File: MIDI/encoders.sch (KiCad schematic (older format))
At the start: 47 parts, among them U3 40106, U4 ENCODER_w_SWITCH, U5 ENCODER_w_SWITCH, U6 ENCODER_w_SWITCH

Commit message: Se continuan las correciones correspondientes a la 1ra revisión
> Se realizan los cambios necesarios para la utilización de la biblioteca de huellas autocontenidas.
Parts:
- C10, C11, C12, C13, C14, C15, C16, C4, C5, C6, C7, C8, C9: footprint Capacitors_SMD:C_0603_HandSoldering -> MIDI:C_0805_HandSoldering
- R10, R11, R12, R13, R14, R15, R16, R17, R18, R19, R20, R21, R22, R23, R24, R25, R26, R27, R28, R29, R30, R31, R32, R33, R34, R35, R36, R37, R8, R9: footprint Resistors_SMD:R_0603_HandSoldering -> MIDI:R_0805_HandSoldering
- U3: footprint Housings_DIP:DIP-14_W7.62mm_LongPads -> MIDI:DIP-14_W7.62mm_LongPads

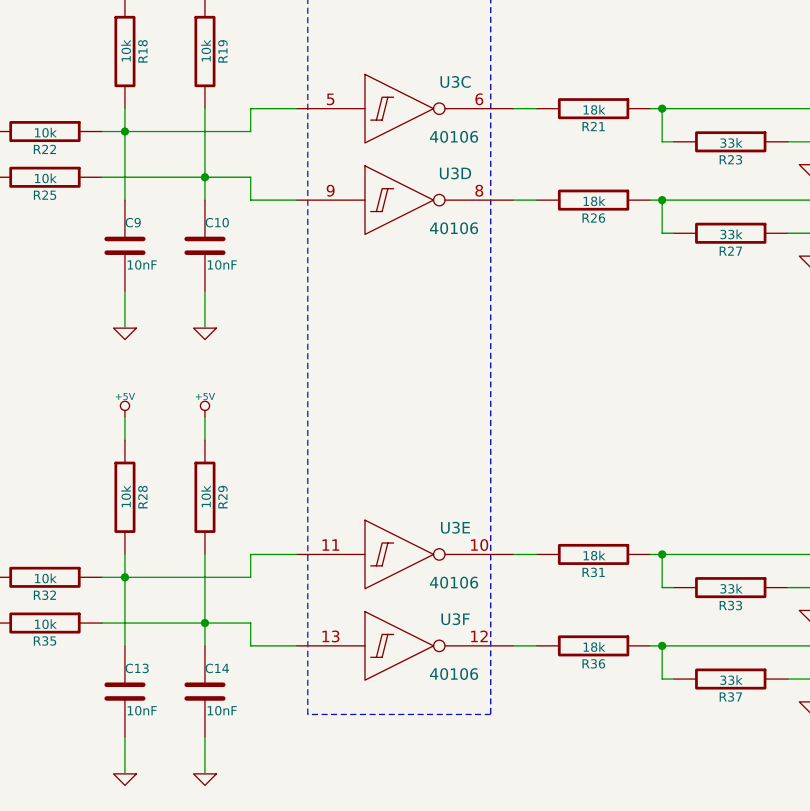
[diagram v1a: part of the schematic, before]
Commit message: Se avanza con primera iteración de ruteo
> Se terminan de rutear conexiones para estudiar factibilidad de placement.
> Para facilitar el ruteo se realizan los siguientes cambios:
  > Se desconecta pin redundante de tact-switch's para permitir la conexión entre planos de masa.
  > Se desconectan pines del conector derecho de forma que no requieran ser ruteados a los homologos del conector izquierdo.
  > Se intercambian unidades F y D del componente 40106.
  > Se agrupan señales de los interruptores de los encoders en vez de intercalarlos con las señales de encoder, propiamente dicho, de cada uno. Se rutean a pines superiores en el conector izquierdo, mientras se desplazan las restantes señales hacia abajo.

> Se aguarda comentarios de los revisores para emprolijar, embellecer y mejorar el ruteo.
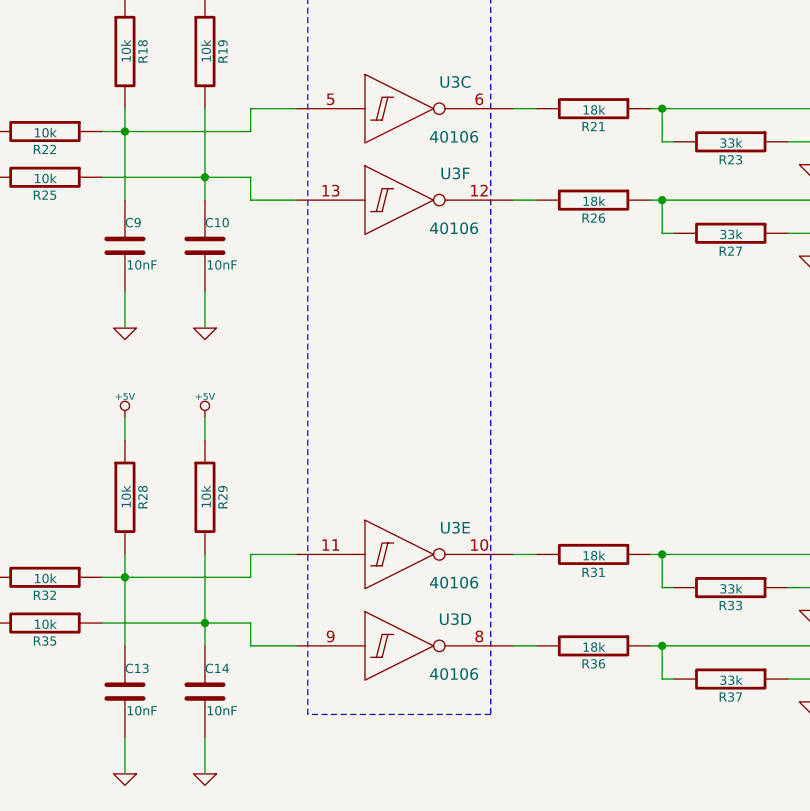
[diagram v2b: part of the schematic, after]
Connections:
- net at U3.8: now also R36.2; no longer R26.2
- net at C10.1, R19.2, R25.1: now also U3.13; no longer U3.9
- net at U3.12: now also R26.2; no longer R36.2
- net at C14.1, R29.2, R35.1: now also U3.9; no longer U3.13
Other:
- moved on the sheet: U3D, U3F

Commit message: Se modifican campos de componentes
> Se realizan los cambios en los campos de kiCost para reflejar los cambios de footprints (de 0603 a 0805).
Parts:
- C10, C13, C14, C5, C6, C9: Desc CAP CER 10000PF 50V X7R 0603 -> CAP CER 10000PF 50V X7R 0805; Digikey# 490-1512-1-ND -> 311-1136-1-ND; Manf Murata Electronics North America -> Yageo; Manf# GRM188R71H103KA01D -> CC0805KRX7R9BB103; Mouser# 81-GRM39X103K50D -> 603-CC805KRX7R9BB103
- C11, C12, C15, C16, C4, C7, C8: Desc CAP CER 0.1UF 16V X7R 0603 -> CAP CER 0.1UF 50V X7R 0805; Digikey# 490-1532-1-ND -> 311-1140-1-ND; Manf Murata Electronics North America -> Yageo; Manf# GRM188R71C104KA01D -> CC0805KRX7R9BB104; Mouser# 81-GRM39X104K16 -> 603-CC805KRX7R9BB104
- R10, R12, R15, R18, R19, R20, R22, R25, R28, R29, R30, R32, R35, R8, R9: Desc RES SMD 10K OHM 5% 1/4W 0603 -> RES SMD 10K OHM 5% 1/8W 0805; Digikey# RHM10KDCT-ND -> 311-10KARCT-ND; Manf Rohm Semiconductor -> Yageo; Manf# ESR03EZPJ103 -> RC0805JR-0710KL; Mouser# 755-ESR03EZPJ103 -> 603-RC0805JR-0710KL
- R11, R16, R21, R26, R31, R36: Desc RES SMD 18K OHM 5% 1/4W 0603 -> RES SMD 18K OHM 5% 1/8W 0805; Digikey# RHM18KDCT-ND -> 311-18KARCT-ND; Manf Rohm Semiconductor -> Yageo; Manf# ESR03EZPJ183 -> RC0805JR-0718KL; Mouser# 755-ESR03EZPJ183 -> 603-RC0805JR-0718KL
- R13, R17, R23, R27, R33, R37: Desc RES SMD 33K OHM 5% 1/4W 0603 -> RES SMD 33K OHM 1% 1/8W 0805; Digikey# RHM33KDCT-ND -> 311-33.0KCRCT-ND; Manf Rohm Semiconductor -> Yageo; Manf# ESR03EZPJ333 -> RC0805FR-0733KL; Mouser# 755-ESR03EZPJ333 -> 603-RC0805FR-0733KL
- R14, R24, R34: Desc RES SMD 1K OHM 5% 1/4W 0603 -> RES SMD 1K OHM 5% 1/8W 0805; Digikey# RHM1.0KDCT-ND -> 311-1.0KARCT-ND; Manf Rohm Semiconductor -> Yageo; Manf# ESR03EZPJ102 -> RC0805JR-071KL; Mouser# 755-ESR03EZPJ102 -> 603-RC0805JR-071KL

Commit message: Correcciones menores en campos para BOM
> Se corrigen error observados luego de la generación de la BOM.
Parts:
- C10, C13, C14, C5, C6, C9: Description (none) -> CAP CER 10000PF 50V X7R 0805
- C11, C12, C15, C16, C4, C7, C8: Description (none) -> CAP CER 0.1UF 50V X7R 0805
- R10, R12, R15, R18, R19, R20, R22, R25, R28, R29, R30, R32, R35, R8, R9: Description (none) -> RES SMD 10K OHM 5% 1/8W 0805
- R11, R16, R21, R26, R31, R36: Description (none) -> RES SMD 18K OHM 5% 1/8W 0805
- R13, R17, R23, R27, R33, R37: Description (none) -> RES SMD 33K OHM 1% 1/8W 0805
- R14, R24, R34: Description (none) -> RES SMD 1K OHM 5% 1/8W 0805
- U3: Desc IC INVERTER GATE HEX 14DIP -> IC INVERTER GATE HEX 14DIP; Description (none) -> IC INVERTER GATE HEX 14DIP
- U4, U5, U6: Description (none) -> ENCODER LO PROFILE 11MM W/SWITCH
